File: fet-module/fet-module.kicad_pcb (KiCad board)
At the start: 2 copper layers, 80 x 22 mm, 30 parts

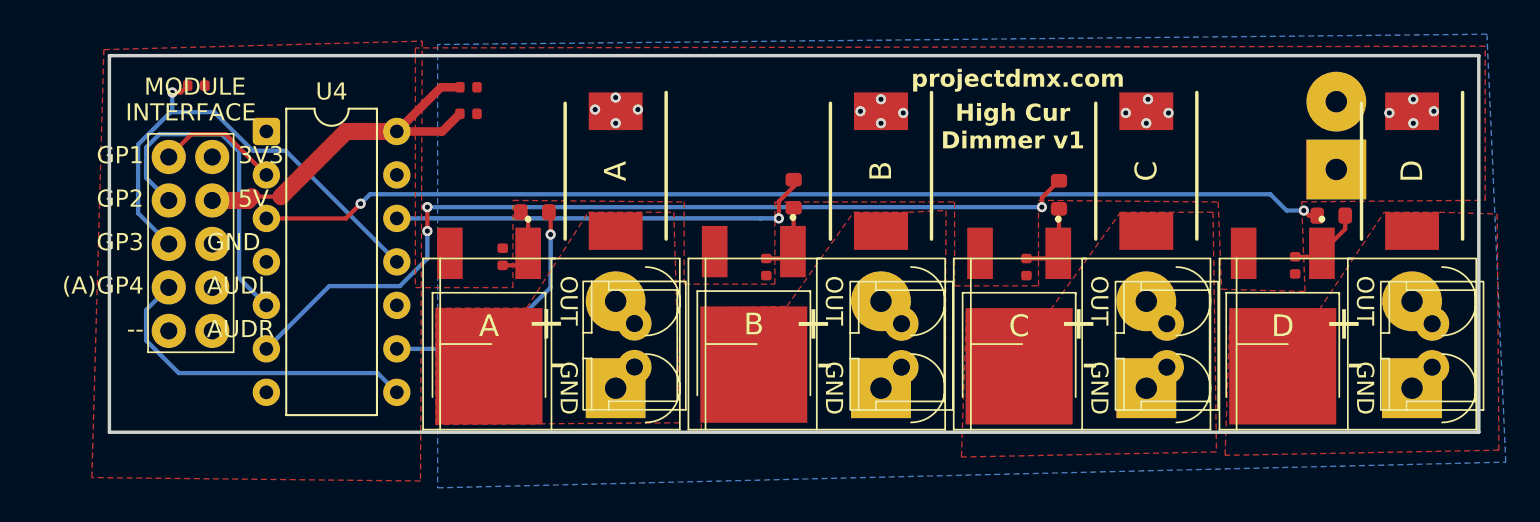
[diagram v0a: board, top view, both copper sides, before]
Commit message: move mounting holes on modules and controller
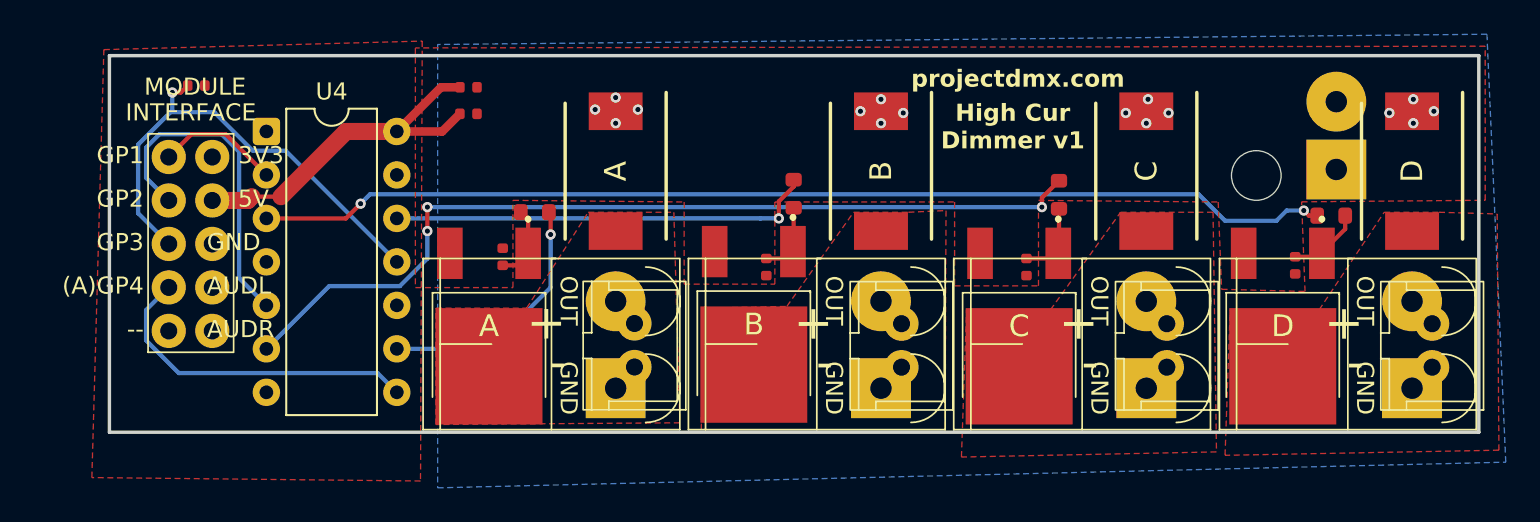
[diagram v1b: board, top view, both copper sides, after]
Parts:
- added ?: , , F.Cu at (200.8, 80.4)
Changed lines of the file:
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@@
 			(fill no)
 			(layer "F.SilkS")
-			(net 56)
 		)
 		(fp_text user "AUDR"
@@
 		)
 	)
+	(footprint ""
+		(layer "F.Cu")
+		(at 200.8255 80.351)
+		(property "Reference" ""
+			(at 0 0 0)
+			(layer "F.SilkS")
+			(effects
+				(font
+					(size 1.27 1.27)
+					(thickness 0.15)
+				)
+			)
+		)
+		(property "Value" ""
+			(at 0 0 0)
+			(layer "F.Fab")
+			(effects
+				(font
+					(size 1.27 1.27)
+					(thickness 0.15)
+				)
+			)
+		)
+		(property "Datasheet" ""
+			(at 0 0 0)
+			(layer "F.Fab")
+			(hide yes)
+			(effects
+				(font
+					(size 1.27 1.27)
+					(thickness 0.15)
+				)
+			)
+		)
+		(property "Description" ""
+			(at 0 0 0)
+			(layer "F.Fab")
+			(hide yes)
+			(effects
+				(font
+					(size 1.27 1.27)
+					(thickness 0.15)
+				)
+			)
+		)
+		(pad "" np_thru_hole circle
+			(at -13 7)
+			(size 2.9 2.9)
+			(drill 2.9)
+			(layers "*.Cu" "*.Mask")
+		)
+		(embedded_fonts no)
+	)
 	(footprint "PCM_JLCPCB:R_0402"
 		(layer "F.Cu")
@@
 			)
 			(layer "B.SilkS")
-			(net 56)
 		)
 		(fp_line
@@
 			)
 			(layer "B.SilkS")
-			(net 56)
 		)
 		(fp_line
@@
 			)
 			(layer "B.SilkS")
-			(net 56)
 		)
 		(fp_line
@@
 			)
 			(layer "B.SilkS")
-			(net 56)
 		)
 		(fp_line
@@
 			)
 			(layer "B.SilkS")
-			(net 56)
 		)
 		(fp_rect
@@
 			(fill no)
 			(layer "B.SilkS")
-			(net 56)
 		)
 		(fp_text user "-"
@@
 	)
 	(segment
+		(start 184.446 88.446)
+		(end 136.054 88.446)
+		(width 0.25)
+		(layer "B.Cu")
+		(net 5)
+	)
+	(segment
+		(start 186 90)
+		(end 184.446 88.446)
+		(width 0.25)
+		(layer "B.Cu")
+		(net 5)
+	)
+	(segment
 		(start 190.6 89.4)
 		(end 189.6 89.4)
@@
 	(segment
 		(start 189.6 89.4)
-		(end 188.646 88.446)
+		(end 189 90)
+		(width 0.25)
+		(layer "B.Cu")
+		(net 5)
+	)
+	(segment
+		(start 189 90)
+		(end 186 90)
 		(width 0.25)
 		(layer "B.Cu")
@@
 		(start 136.054 88.446)
 		(end 135.5 89)
-		(width 0.25)
-		(layer "B.Cu")
-		(net 5)
-	)
-	(segment
-		(start 188.646 88.446)
-		(end 136.054 88.446)
 		(width 0.25)
 		(layer "B.Cu")
@@
 		(polygon
 			(pts
-				(xy 120.5 80) (xy 139.1 79.5) (xy 139 105.2) (xy 119.8 105) (xy 120.5 80)
-			)
-		)
+				(xy 120.5 80) (xy 139.1 79.5) (xy 139 105.2) (xy 119.8 105)
+			)
+		)

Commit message: adjust footprints and cleanup stuff
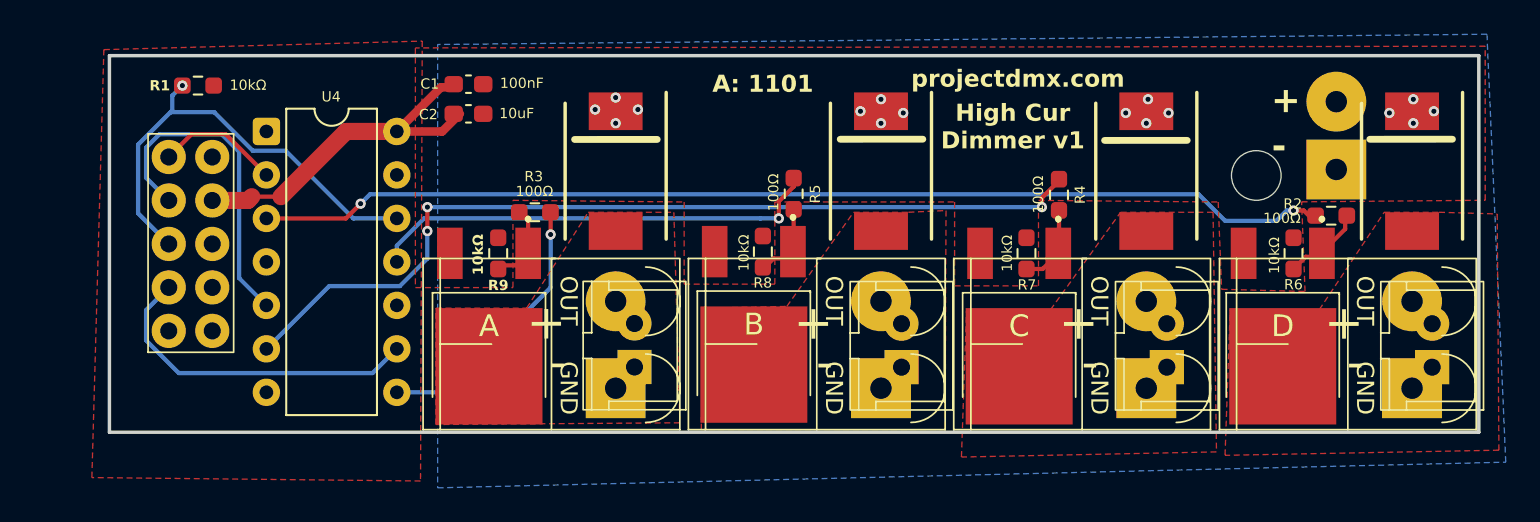
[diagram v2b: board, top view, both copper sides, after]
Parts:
- C1, C2: footprint PCM_JLCPCB:C_0402 -> Capacitor_SMD:C_0603_1608Metric_Pad1.08x0.95mm_HandSolder
- R1, R6, R7, R8, R9: footprint PCM_JLCPCB:R_0402 -> Resistor_SMD:R_0603_1608Metric_Pad0.98x0.95mm_HandSolder
- R2, R3, R4, R5: footprint PCM_JLCPCB:R_0603 -> Resistor_SMD:R_0603_1608Metric_Pad0.98x0.95mm_HandSolder
- moved R8 0.92 mm to (159.0, 91.8), turned to -90 degrees
- moved R7 0.80 mm to (174.4, 91.9), turned to -90 degrees
- moved R6 0.71 mm to (190.0, 91.9), turned to -90 degrees
- moved R9 0.33 mm to (143.5, 91.9)
- moved C1 0.18 mm to (141.8, 82.0)
- moved R1 0.10 mm to (126.0, 82.1)
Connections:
- U4 pad 11: Net-(U4-4A_(In)) -> Net-(U4-4Y_(Out))
- U4 pad 12: Net-(U4-4Y_(Out)) -> Net-(U4-4A_(In))
- U4 pad 8: Net-(U4-3A_(In)) -> Net-(U4-2Y_(Out))
- U4 pad 9: Net-(U4-2Y_(Out)) -> Net-(U4-3A_(In))
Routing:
- net Net-(U4-4Y_(Out)): track 29.2 -> 31.5 mm
- net Net-(U4-2Y_(Out)): track 19.6 -> 21.0 mm
- net Net-(U4-4A_(In)): track 28.3 -> 27.2 mm
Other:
- board text added: "+"
- board text added: "-"
- board text added: "A: 1101"

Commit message: cleanup footprints and layout
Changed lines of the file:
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@@
 	)
 	(gr_text "A: 1101"
-		(at 159 82 0)
+		(at 122.189538 91.396099 90)
 		(layer "F.SilkS")
 		(effects
